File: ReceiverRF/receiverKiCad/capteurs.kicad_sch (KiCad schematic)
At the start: 10 parts, among them J3 Conn_01x04, U4 MLX90393SLW-ABA-011-RE

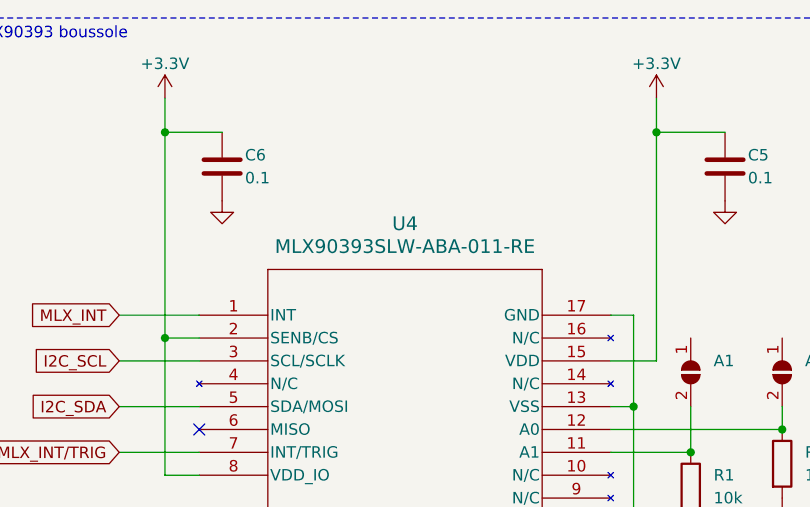
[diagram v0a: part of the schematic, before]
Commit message: Changement régulateurs, meilleur circuit debouncing boutons, documentation
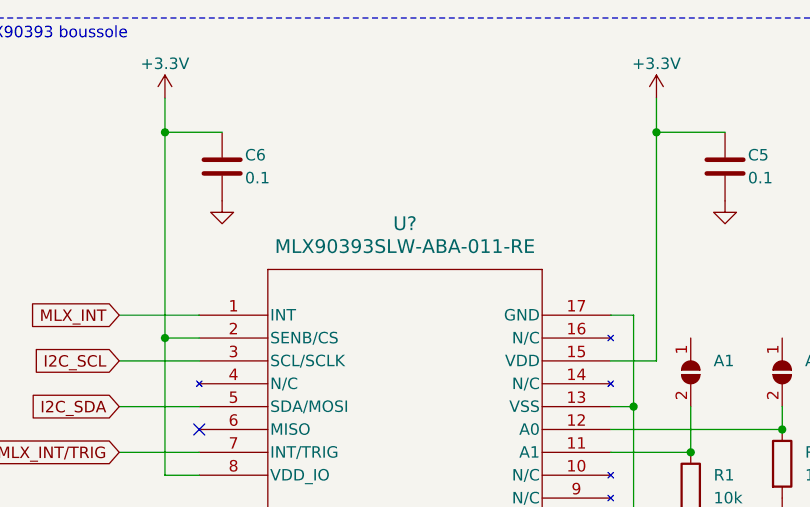
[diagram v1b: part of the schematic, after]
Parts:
- removed U4: MLX90393SLW-ABA-011-RE, QFN-16_MLX90393_MEL, symbol symbol-receiver:MLX90393SLW-ABA-011-RE
- added U?: MLX90393SLW-ABA-011-RE, QFN-16_MLX90393_MEL, symbol symbol-receiver:MLX90393SLW-ABA-011-RE
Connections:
- net +3.3V: now also U?.15 (VDD), U?.2 (SENB/CS), U?.8 (VDD_IO)
- net GND: now also U?.13 (VSS), U?.17 (GND)
- net I2C_SCL: now also U?.3 (SCL/SCLK)
- net I2C_SDA: now also U?.5 (SDA/MOSI)
- net MLX_INT: now also U?.1 (INT)
- net MLX_INT/TRIG: now also U?.7 (INT/TRIG)
- net at A1.2 (B), R1.1: now also U?.11 (A1)
- net at A0.2 (B), R2.1: now also U?.12 (A0)
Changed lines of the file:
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@@
-    )
-  )
-  (symbol (lib_id "power:+5V") (at 49.53 149.86 0) (unit 1)
-    (in_bom yes) (on_board yes) (dnp no) (fields_autoplaced)
-    (property "Reference" "#PWR019" (at 49.53 153.67 0)
-      (effects (font (size 1.27 1.27)) hide)
-    )
-    (property "Value" "+5V" (at 49.53 144.78 0)
-      (effects (font (size 1.27 1.27)))
-    )
-    (property "Footprint" "" (at 49.53 149.86 0)
-      (effects (font (size 1.27 1.27)) hide)
-    )
-    (property "Datasheet" "" (at 49.53 149.86 0)
-      (effects (font (size 1.27 1.27)) hide)
-    )
-    (pin "1")
-    (instances
-      (project "receiver"
-        (path "/439ba515-58d4-4b14-87ab-b438dcf423a5"
-          (reference "#PWR019") (unit 1)
-        )
-        (path "/439ba515-58d4-4b14-87ab-b438dcf423a5/56b56711-4d65-4df6-9470-6736a83e438d"
-          (reference "#PWR019") (unit 1)
-        )
-      )
     )
   )
   (symbol (lib_id "symbol-receiver:MLX90393SLW-ABA-011-RE") (at 44.45 52.07 0) (unit 1)
     (in_bom yes) (on_board yes) (dnp no) (fields_autoplaced)
-    (property "Reference" "U4" (at 67.31 41.91 0)
+    (property "Reference" "U?" (at 67.31 41.91 0)
       (effects (font (size 1.524 1.524)))
     )
@@
       (project "receiver"
         (path "/439ba515-58d4-4b14-87ab-b438dcf423a5/56b56711-4d65-4df6-9470-6736a83e438d"
-          (reference "U4") (unit 1)
+          (reference "U?") (unit 1)
         )
       )
+    )
+  )
+  (symbol (lib_id "power:+5V") (at 49.53 149.86 0) (unit 1)
+    (in_bom yes) (on_board yes) (dnp no) (fields_autoplaced)
+    (property "Reference" "#PWR019" (at 49.53 153.67 0)
+      (effects (font (size 1.27 1.27)) hide)
+    )
+    (property "Value" "+5V" (at 49.53 144.78 0)
+      (effects (font (size 1.27 1.27)))
+    )
+    (property "Footprint" "" (at 49.53 149.86 0)
+      (effects (font (size 1.27 1.27)) hide)
+    )
+    (property "Datasheet" "" (at 49.53 149.86 0)
+      (effects (font (size 1.27 1.27)) hide)
+    )
+    (pin "1")
+    (instances
+      (project "receiver"
+        (path "/439ba515-58d4-4b14-87ab-b438dcf423a5"
+          (reference "#PWR019") (unit 1)
+        )
+        (path "/439ba515-58d4-4b14-87ab-b438dcf423a5/56b56711-4d65-4df6-9470-6736a83e438d"
+          (reference "#PWR019") (unit 1)
+        )
+      )

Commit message: To kicad 8
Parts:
- renumbered J3 to J?

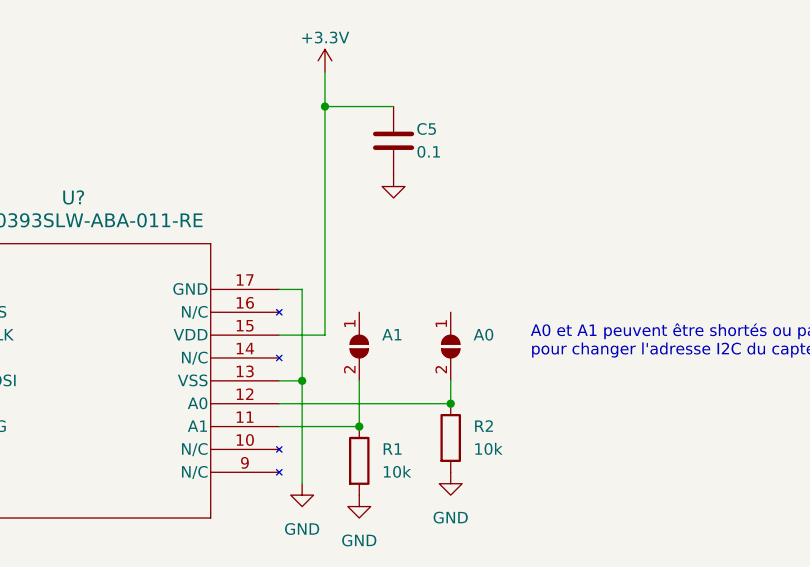
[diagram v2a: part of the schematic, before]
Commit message: Corrige path footprints
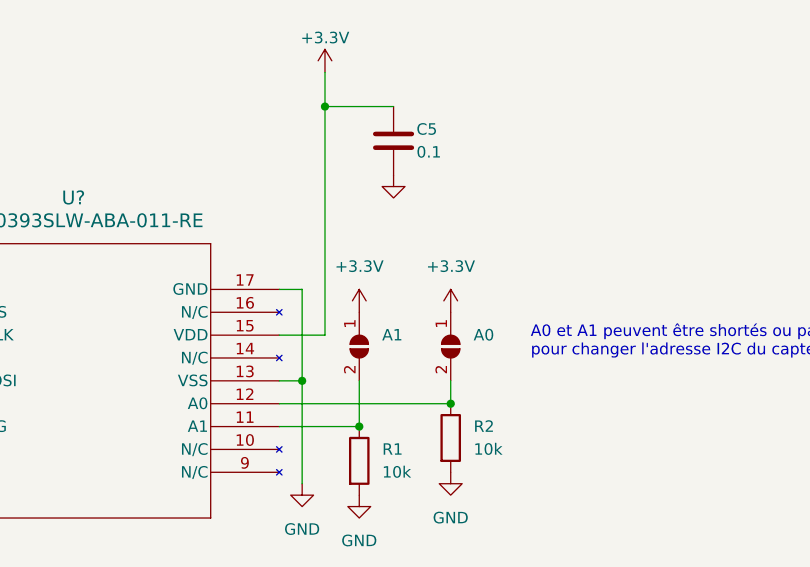
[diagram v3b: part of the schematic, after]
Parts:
- J?: footprint footprint-receiver:CONN_RF2-04A-T-00-50-G_ADM -> (none)
- RF1: footprint (none) -> Footprints:RFM22b-S2
- U?: footprint QFN-16_MLX90393_MEL -> Footprints:QFN-16_MLX90393_MEL-L
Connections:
- net +3.3V: now also A0.1 (A), A1.1 (A)
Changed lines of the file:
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@@
 			)
 		)
-		(property "Footprint" "QFN-16_MLX90393_MEL"
+		(property "Footprint" "Footprints:QFN-16_MLX90393_MEL-L"
 			(at 36.83 49.53 0)
 			(effects
@@
 			)
 		)
-		(property "Footprint" ""
+		(property "Footprint" "Footprints:RFM22b-S2"
 			(at 44.45 106.68 0)
 			(effects
@@
 				(path "/439ba515-58d4-4b14-87ab-b438dcf423a5/56b56711-4d65-4df6-9470-6736a83e438d"
 					(reference "RF1")
+					(unit 1)
+				)
+			)
+		)
+	)
+	(symbol
+		(lib_name "+3.3V_1")
+		(lib_id "power:+3.3V")
+		(at 109.22 54.61 0)
+		(unit 1)
+		(exclude_from_sim no)
+		(in_bom yes)
+		(on_board yes)
+		(dnp no)
+		(fields_autoplaced yes)
+		(property "Reference" "#PWR060"
+			(at 109.22 58.42 0)
+			(effects
+				(font
+					(size 1.27 1.27)
+				)
+				(hide yes)
+			)
+		)
+		(property "Value" "+3.3V"
+			(at 109.22 49.53 0)
+			(effects
+				(font
+					(size 1.27 1.27)
+				)
+			)
+		)
+		(property "Footprint" ""
+			(at 109.22 54.61 0)
+			(effects
+				(font
+					(size 1.27 1.27)
+				)
+				(hide yes)
+			)
+		)
+		(property "Datasheet" ""
+			(at 109.22 54.61 0)
+			(effects
+				(font
+					(size 1.27 1.27)
+				)
+				(hide yes)
+			)
+		)
+		(property "Description" "Power symbol creates a global label with name \"+3.3V\""
+			(at 109.22 54.61 0)
+			(effects
+				(font
+					(size 1.27 1.27)
+				)
+				(hide yes)
+			)
+		)
+		(pin "1"
+		)
+		(instances
+			(project "receiver"
+				(path "/439ba515-58d4-4b14-87ab-b438dcf423a5/56b56711-4d65-4df6-9470-6736a83e438d"
+					(reference "#PWR060")
 					(unit 1)
 				)
@@
 	)
 	(symbol
+		(lib_name "+3.3V_1")
+		(lib_id "power:+3.3V")
+		(at 99.06 54.61 0)
+		(unit 1)
+		(exclude_from_sim no)
+		(in_bom yes)
+		(on_board yes)
+		(dnp no)
+		(fields_autoplaced yes)
+		(property "Reference" "#PWR059"
+			(at 99.06 58.42 0)
+			(effects
+				(font
+					(size 1.27 1.27)
+				)
+				(hide yes)
+			)
+		)
+		(property "Value" "+3.3V"
+			(at 99.06 49.53 0)
+			(effects
+				(font
+					(size 1.27 1.27)
+				)
+			)
+		)
+		(property "Footprint" ""
+			(at 99.06 54.61 0)
+			(effects
+				(font
+					(size 1.27 1.27)
+				)
+				(hide yes)
+			)
+		)
+		(property "Datasheet" ""
+			(at 99.06 54.61 0)
+			(effects
+				(font
+					(size 1.27 1.27)
+				)
+				(hide yes)
+			)
+		)
+		(property "Description" "Power symbol creates a global label with name \"+3.3V\""
+			(at 99.06 54.61 0)
+			(effects
+				(font
+					(size 1.27 1.27)
+				)
+				(hide yes)
+			)
+		)
+		(pin "1"
+		)
+		(instances
+			(project "receiver"
+				(path "/439ba515-58d4-4b14-87ab-b438dcf423a5/56b56711-4d65-4df6-9470-6736a83e438d"
+					(reference "#PWR059")
+					(unit 1)
+				)
+			)
+		)
+	)
+	(symbol
 		(lib_id "power:GND")
 		(at 92.71 73.66 0)
@@
 			)
 		)
-		(property "Footprint" "footprint-receiver:CONN_RF2-04A-T-00-50-G_ADM"
+		(property "Footprint" ""
 			(at 25.4 107.95 0)
 			(effects
@@
 			)
 		)
-		(property "Datasheet" " ~"
+		(property "Datasheet" "~"
 			(at 25.4 107.95 0)
 			(effects

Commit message: Choix cristal 8MHz et Connecteur SMA. Footprint et documentation
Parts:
- J?: footprint (none) -> Footprints:SMA_90deg
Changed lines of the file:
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@@
 			)
 		)
-		(property "Footprint" ""
+		(property "Footprint" "Footprints:SMA_90deg"
 			(at 25.4 107.95 0)
 			(effects
@@
 			)
 		)
-		(property "Datasheet" "~"
+		(property "Datasheet" "https://www.digikey.ca/en/products/detail/adam-tech/RF2-03E-T-00-50-G/9831386"
 			(at 25.4 107.95 0)
 			(effects

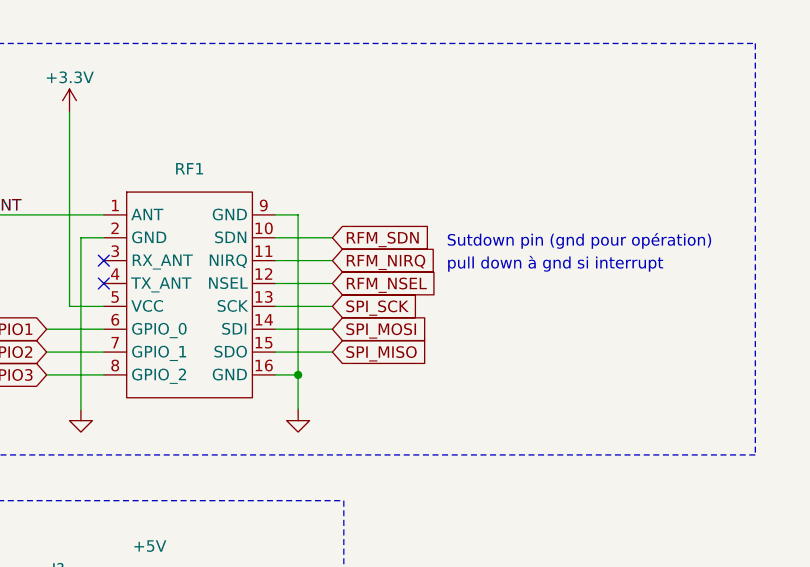
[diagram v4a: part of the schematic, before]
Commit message: Buzzer et diode. Toutes les pièces importantes sont choisies et footprint
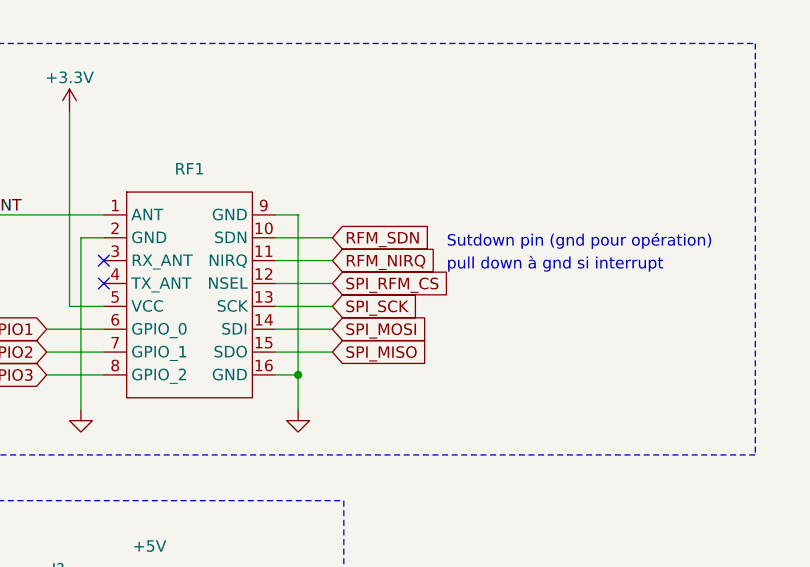
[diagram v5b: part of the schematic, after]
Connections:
- net RFM_NSEL renamed SPI_RFM_CS
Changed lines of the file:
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@@
 		)
 	)
-	(global_label "RFM_NSEL"
+	(global_label "SPI_RFM_CS"
 		(shape input)
 		(at 69.85 115.57 0)
@@
 		)
 		(property "Intersheetrefs" "${INTERSHEET_REFS}"
-			(at 82.3299 115.57 0)
+			(at 84.1442 115.57 0)
 			(effects
 				(font

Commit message: Identifiants des symboles
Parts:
- gave numbers to parts that had none: 3
- renumbered A0 to MLX_A0, A1 to MLX_A1, C6 to MLX_C1, C5 to MLX_C2, R2 to MLX_R1, R1 to MLX_R2
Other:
- moved on the sheet: MLX_A0, MLX_R1
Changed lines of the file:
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@@
 	)
 	(junction
-		(at 109.22 64.77)
+		(at 110.49 64.77)
 		(diameter 0)
 		(color 0 0 0 0)
@@
 	(wire
 		(pts
+			(xy 90.17 64.77) (xy 110.49 64.77)
+		)
+		(stroke
+			(width 0)
+			(type default)
+		)
+	)
+	(wire
+		(pts
 			(xy 40.64 27.94) (xy 40.64 31.75)
 		)
@@
 	(wire
 		(pts
-			(xy 90.17 64.77) (xy 109.22 64.77)
-		)
-		(stroke
-			(width 0)
-			(type default)
-		)
-	)
-	(wire
-		(pts
 			(xy 90.17 52.07) (xy 92.71 52.07)
 		)
@@
 	(wire
 		(pts
-			(xy 109.22 62.23) (xy 109.22 64.77)
+			(xy 110.49 62.23) (xy 110.49 64.77)
 		)
 		(stroke
@@
 	(text "A0 et A1 peuvent être shortés ou pas,\npour changer l'adresse I2C du capteur"
 		(exclude_from_sim no)
-		(at 118.11 59.69 0)
+		(at 121.158 60.198 0)
 		(effects
 			(font
@@
 		(on_board yes)
 		(dnp no)
-		(fields_autoplaced yes)
-		(property "Reference" "R1"
-			(at 101.6 69.85 0)
+		(property "Reference" "MLX_R2"
+			(at 101.346 69.85 0)
 			(effects
 				(font
@@
 			(project "receiver"
 				(path "/439ba515-58d4-4b14-87ab-b438dcf423a5/56b56711-4d65-4df6-9470-6736a83e438d"
-					(reference "R1")
+					(reference "MLX_R2")
 					(unit 1)
 				)
@@
 	(symbol
 		(lib_id "Jumper:SolderJumper_2_Open")
-		(at 109.22 58.42 270)
+		(at 110.49 58.42 270)
 		(unit 1)
 		(exclude_from_sim no)
@@
 		(on_board yes)
 		(dnp no)
-		(fields_autoplaced yes)
-		(property "Reference" "A0"
-			(at 111.76 57.15 90)
+		(property "Reference" "MLX_A0"
+			(at 112.014 56.896 90)
 			(effects
 				(font
@@
 		)
 		(property "Value" "0"
-			(at 111.76 59.69 90)
+			(at 113.03 59.69 90)
 			(effects
 				(font
@@
 		)
 		(property "Footprint" ""
-			(at 109.22 58.42 0)
+			(at 110.49 58.42 0)
 			(effects
 				(font
@@
 		)
 		(property "Datasheet" "~"
-			(at 109.22 58.42 0)
+			(at 110.49 58.42 0)
 			(effects
 				(font
@@
 		)
 		(property "Description" ""
-			(at 109.22 58.42 0)
+			(at 110.49 58.42 0)
 			(effects
 				(font
@@
 			(project "receiver"
 				(path "/439ba515-58d4-4b14-87ab-b438dcf423a5/56b56711-4d65-4df6-9470-6736a83e438d"
-					(reference "A0")
+					(reference "MLX_A0")
 					(unit 1)
 				)
@@
 	(symbol
 		(lib_id "Device:R")
-		(at 109.22 68.58 0)
+		(at 110.49 68.58 0)
 		(unit 1)
 		(exclude_from_sim no)
@@
 		(dnp no)
 		(fields_autoplaced yes)
-		(property "Reference" "R2"
-			(at 111.76 67.31 0)
+		(property "Reference" "MLX_R1"
+			(at 113.03 67.31 0)
 			(effects
 				(font
@@
 		)
 		(property "Value" "10k"
-			(at 111.76 69.85 0)
+			(at 113.03 69.85 0)
 			(effects
 				(font
@@
 		)
 		(property "Footprint" ""
-			(at 107.442 68.58 90)
+			(at 108.712 68.58 90)
 			(effects
 				(font
@@
 		)
 		(property "Datasheet" "~"
-			(at 109.22 68.58 0)
+			(at 110.49 68.58 0)
 			(effects
 				(font
@@
 		)
 		(property "Description" ""
-			(at 109.22 68.58 0)
+			(at 110.49 68.58 0)
 			(effects
 				(font
@@
 			(project "receiver"
 				(path "/439ba515-58d4-4b14-87ab-b438dcf423a5/56b56711-4d65-4df6-9470-6736a83e438d"
-					(reference "R2")
+					(reference "MLX_R1")
 					(unit 1)
 				)
@@
 		(on_board yes)
 		(dnp no)
-		(property "Reference" "C5"
+		(property "Reference" "MLX_C2"
 			(at 105.41 34.29 0)
 			(effects
@@
 			(project "receiver"
 				(path "/439ba515-58d4-4b14-87ab-b438dcf423a5/56b56711-4d65-4df6-9470-6736a83e438d"
-					(reference "C5")
+					(reference "MLX_C2")
 					(unit 1)
 				)
@@
 		(dnp no)
 		(fields_autoplaced yes)
-		(property "Reference" "U?"
+		(property "Reference" "U4"
 			(at 67.31 41.91 0)
 			(effects
@@
 			(project "receiver"
 				(path "/439ba515-58d4-4b14-87ab-b438dcf423a5/56b56711-4d65-4df6-9470-6736a83e438d"
-					(reference "U?")
+					(reference "U4")
 					(unit 1)
 				)
@@
 		(lib_name "+3.3V_1")
 		(lib_id "power:+3.3V")
-		(at 109.22 54.61 0)
+		(at 110.49 54.61 0)
 		(unit 1)
 		(exclude_from_sim no)
@@
 		(fields_autoplaced yes)
 		(property "Reference" "#PWR060"
-			(at 109.22 58.42 0)
+			(at 110.49 58.42 0)
 			(effects
 				(font
@@
 		)
 		(property "Value" "+3.3V"
-			(at 109.22 49.53 0)
+			(at 110.49 49.53 0)
 			(effects
 				(font
@@
 		)
 		(property "Footprint" ""
-			(at 109.22 54.61 0)
+			(at 110.49 54.61 0)
 			(effects
 				(font
@@
 		)
 		(property "Datasheet" ""
-			(at 109.22 54.61 0)
+			(at 110.49 54.61 0)
 			(effects
 				(font
@@
 		)
 		(property "Description" "Power symbol creates a global label with name \"+3.3V\""
-			(at 109.22 54.61 0)
+			(at 110.49 54.61 0)
 			(effects
 				(font
@@
 		(on_board yes)
 		(dnp no)
-		(property "Reference" "C6"
+		(property "Reference" "MLX_C1"
 			(at 49.53 34.29 0)
 			(effects
@@
 			(project "receiver"
 				(path "/439ba515-58d4-4b14-87ab-b438dcf423a5/56b56711-4d65-4df6-9470-6736a83e438d"
-					(reference "C6")
+					(reference "MLX_C1")
 					(unit 1)
 				)
@@
 	(symbol
 		(lib_id "power:GND")
-		(at 109.22 72.39 0)
+		(at 110.49 72.39 0)
 		(unit 1)
 		(exclude_from_sim no)
@@
 		(fields_autoplaced yes)
 		(property "Reference" "#PWR09"
-			(at 109.22 78.74 0)
+			(at 110.49 78.74 0)
 			(effects
 				(font
@@
 		)
 		(property "Value" "GND"
-			(at 109.22 77.47 0)
+			(at 110.49 77.47 0)
 			(effects
 				(font
@@
 		)
 		(property "Footprint" ""
-			(at 109.22 72.39 0)
+			(at 110.49 72.39 0)
 			(effects
 				(font
@@
 		)
 		(property "Datasheet" ""
-			(at 109.22 72.39 0)
+			(at 110.49 72.39 0)
 			(effects
 				(font
@@
 		)
 		(property "Description" ""
-			(at 109.22 72.39 0)
+			(at 110.49 72.39 0)
 			(effects
 				(font
@@
 		(on_board yes)
 		(dnp no)
-		(fields_autoplaced yes)
-		(property "Reference" "A1"
-			(at 101.6 57.15 90)
+		(property "Reference" "MLX_A1"
+			(at 100.584 56.896 90)
 			(effects
 				(font
@@
 			(project "receiver"
 				(path "/439ba515-58d4-4b14-87ab-b438dcf423a5/56b56711-4d65-4df6-9470-6736a83e438d"
-					(reference "A1")
+					(reference "MLX_A1")
 					(unit 1)
 				)
@@
 		(dnp no)
 		(fields_autoplaced yes)
-		(property "Reference" "J?"
+		(property "Reference" "J3"
 			(at 39.37 147.32 0)
 			(effects
@@
 			(project "receiver"
 				(path "/439ba515-58d4-4b14-87ab-b438dcf423a5/56b56711-4d65-4df6-9470-6736a83e438d"
-					(reference "J?")
+					(reference "J3")
 					(unit 1)
 				)
@@
 		(dnp no)
 		(fields_autoplaced yes)
-		(property "Reference" "J?"
+		(property "Reference" "J1"
 			(at 25.7174 101.6 0)
 			(effects
@@
 			(project "receiver"
 				(path "/439ba515-58d4-4b14-87ab-b438dcf423a5/56b56711-4d65-4df6-9470-6736a83e438d"
-					(reference "J?")
+					(reference "J1")
 					(unit 1)
 				)

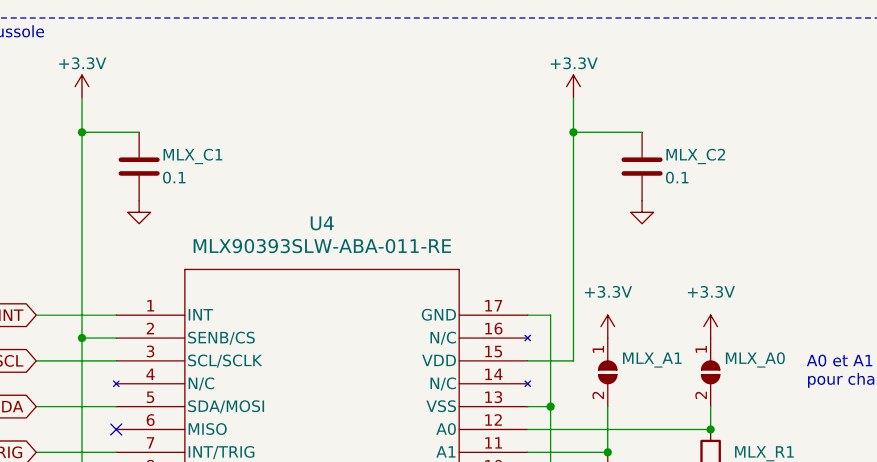
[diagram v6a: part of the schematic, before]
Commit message: Footprint et choix composantes mineures (résistances et condo)
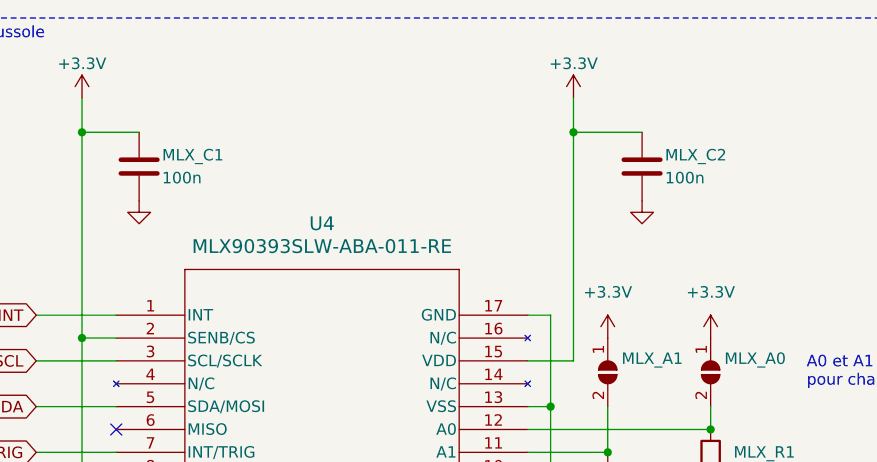
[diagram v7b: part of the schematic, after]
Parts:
- J3: footprint (none) -> Connector_PinHeader_2.00mm:PinHeader_1x04_P2.00mm_Vertical
- MLX_A0, MLX_A1: footprint (none) -> Jumper:SolderJumper-2_P1.3mm_Open_TrianglePad1.0x1.5mm
- MLX_C1, MLX_C2: value 0.1 -> 100n; footprint (none) -> Capacitor_SMD:C_0402_1005Metric
- MLX_R1, MLX_R2: footprint (none) -> Resistor_SMD:R_0402_1005Metric
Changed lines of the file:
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@@
 			)
 		)
-		(property "Footprint" ""
+		(property "Footprint" "Resistor_SMD:R_0402_1005Metric"
 			(at 97.282 71.12 90)
 			(effects
@@
 			)
 		)
-		(property "Footprint" ""
+		(property "Footprint" "Jumper:SolderJumper-2_P1.3mm_Open_TrianglePad1.0x1.5mm"
 			(at 110.49 58.42 0)
 			(effects
@@
 			)
 		)
-		(property "Footprint" ""
+		(property "Footprint" "Resistor_SMD:R_0402_1005Metric"
 			(at 108.712 68.58 90)
 			(effects
@@
 			)
 		)
-		(property "Value" "0.1"
+		(property "Value" "100n"
 			(at 105.41 36.83 0)
 			(effects
@@
 			)
 		)
-		(property "Footprint" ""
+		(property "Footprint" "Capacitor_SMD:C_0402_1005Metric"
 			(at 103.8352 39.37 0)
 			(effects
@@
 			)
 		)
-		(property "Value" "0.1"
+		(property "Value" "100n"
 			(at 49.53 36.83 0)
 			(effects
@@
 			)
 		)
-		(property "Footprint" ""
+		(property "Footprint" "Capacitor_SMD:C_0402_1005Metric"
 			(at 47.9552 39.37 0)
 			(effects
@@
 			)
 		)
-		(property "Footprint" ""
+		(property "Footprint" "Jumper:SolderJumper-2_P1.3mm_Open_TrianglePad1.0x1.5mm"
 			(at 99.06 58.42 0)
 			(effects
@@
 			)
 		)
-		(property "Footprint" ""
+		(property "Footprint" "Connector_PinHeader_2.00mm:PinHeader_1x04_P2.00mm_Vertical"
 			(at 39.37 156.21 0)
 			(effects
